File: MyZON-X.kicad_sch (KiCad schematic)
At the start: 29 parts, among them J1 Connector ZX81, J2 Audio, SW1 SW_DIP_x03, U1 AY-3-8910, U2.1 74HCT74, U3.1 74HCT08, U4.1 74HCT11, U5.1 74HCT02

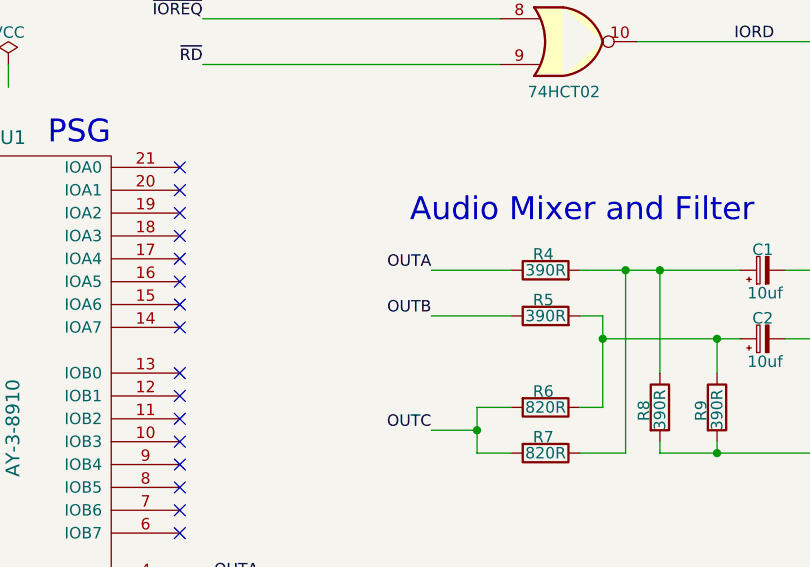
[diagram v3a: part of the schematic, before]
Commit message: Channged Channel A and B over on the audio mixer as they would have been the wrong way to what I intended.
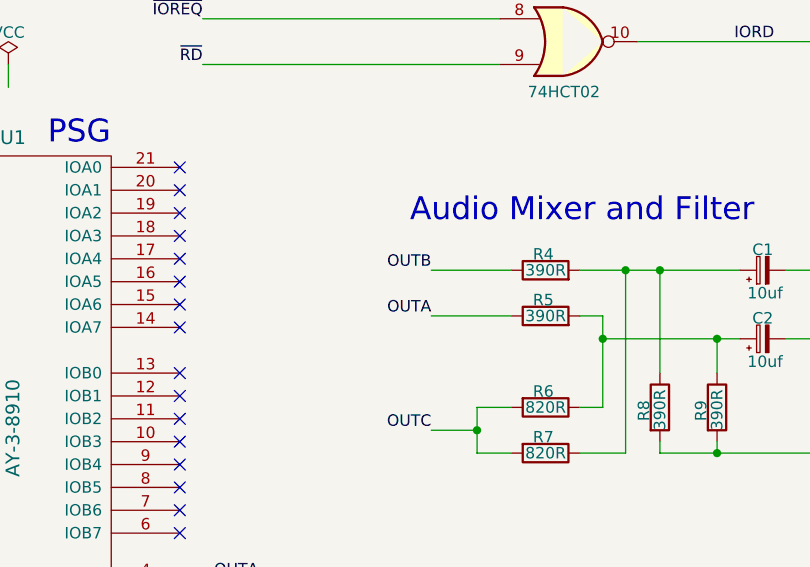
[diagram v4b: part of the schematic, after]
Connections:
- net OUTA: now also R5.1; no longer R4.1
- net OUTB: now also R4.1; no longer R5.1
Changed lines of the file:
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@@
 		)
 	)
-	(label "OUTB"
+	(label "OUTA"
 		(at 130.81 130.81 180)
 		(effects
@@
 		)
 	)
-	(label "OUTA"
+	(label "OUTB"
 		(at 130.81 125.73 180)
 		(effects

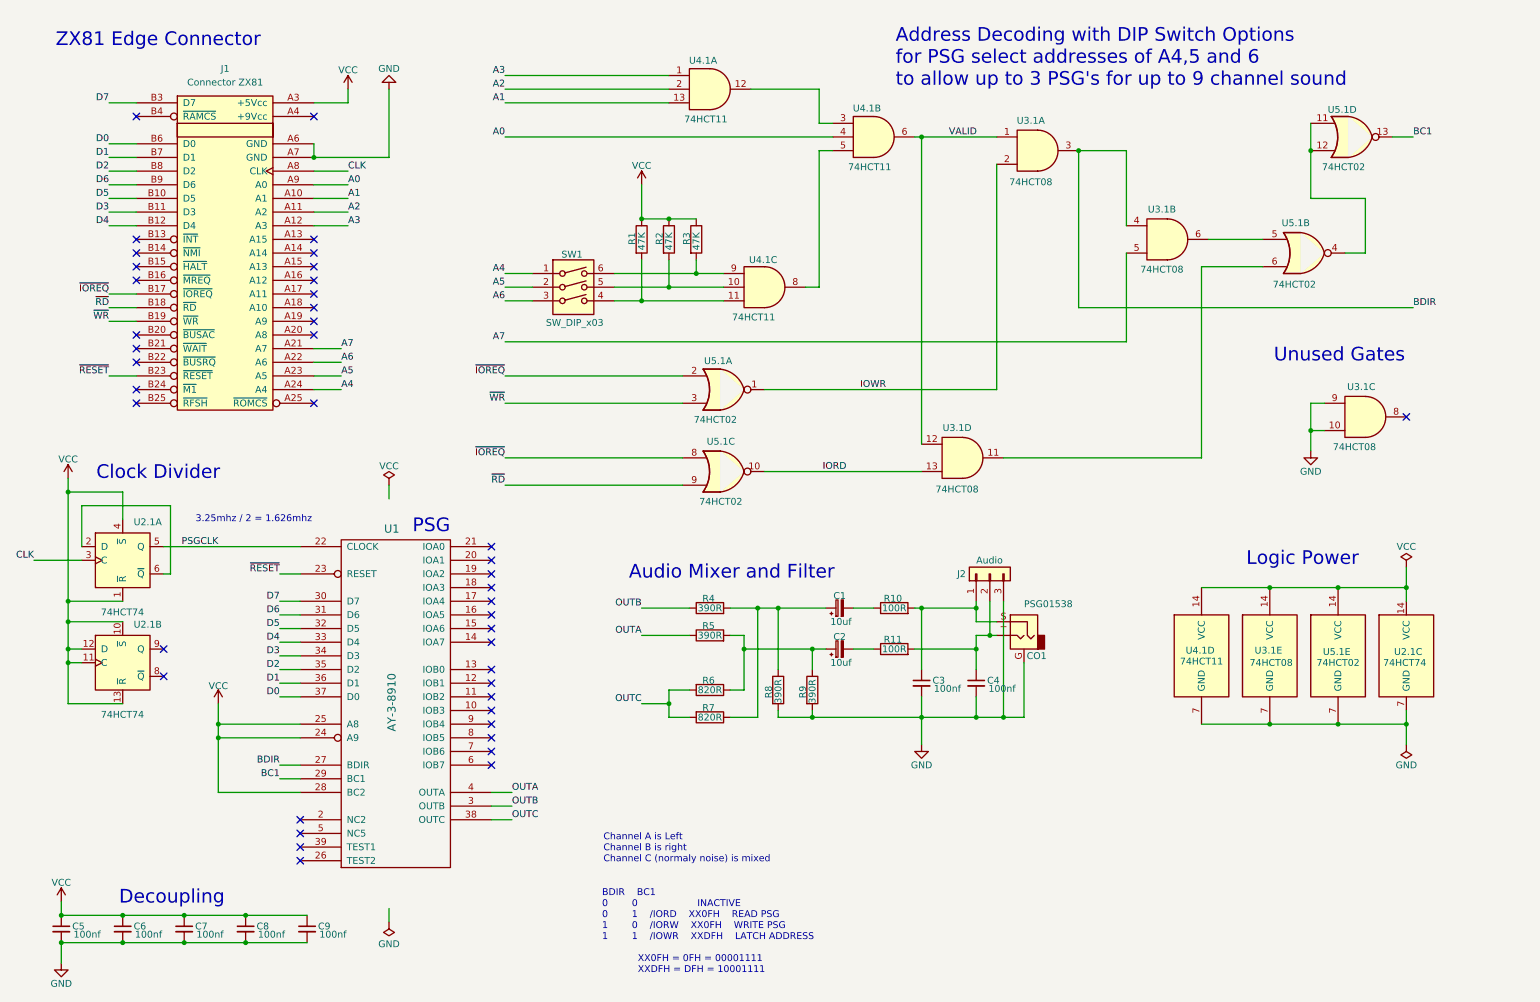
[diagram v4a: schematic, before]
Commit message: added just two power inputs for +5Vcc to VCC and GND to GND Created commented ERC warning as +5Vcc and GND are bidirectional  by design. Move a few of the text comments to make the schematic look neater Exported an updated PDF of the schematic
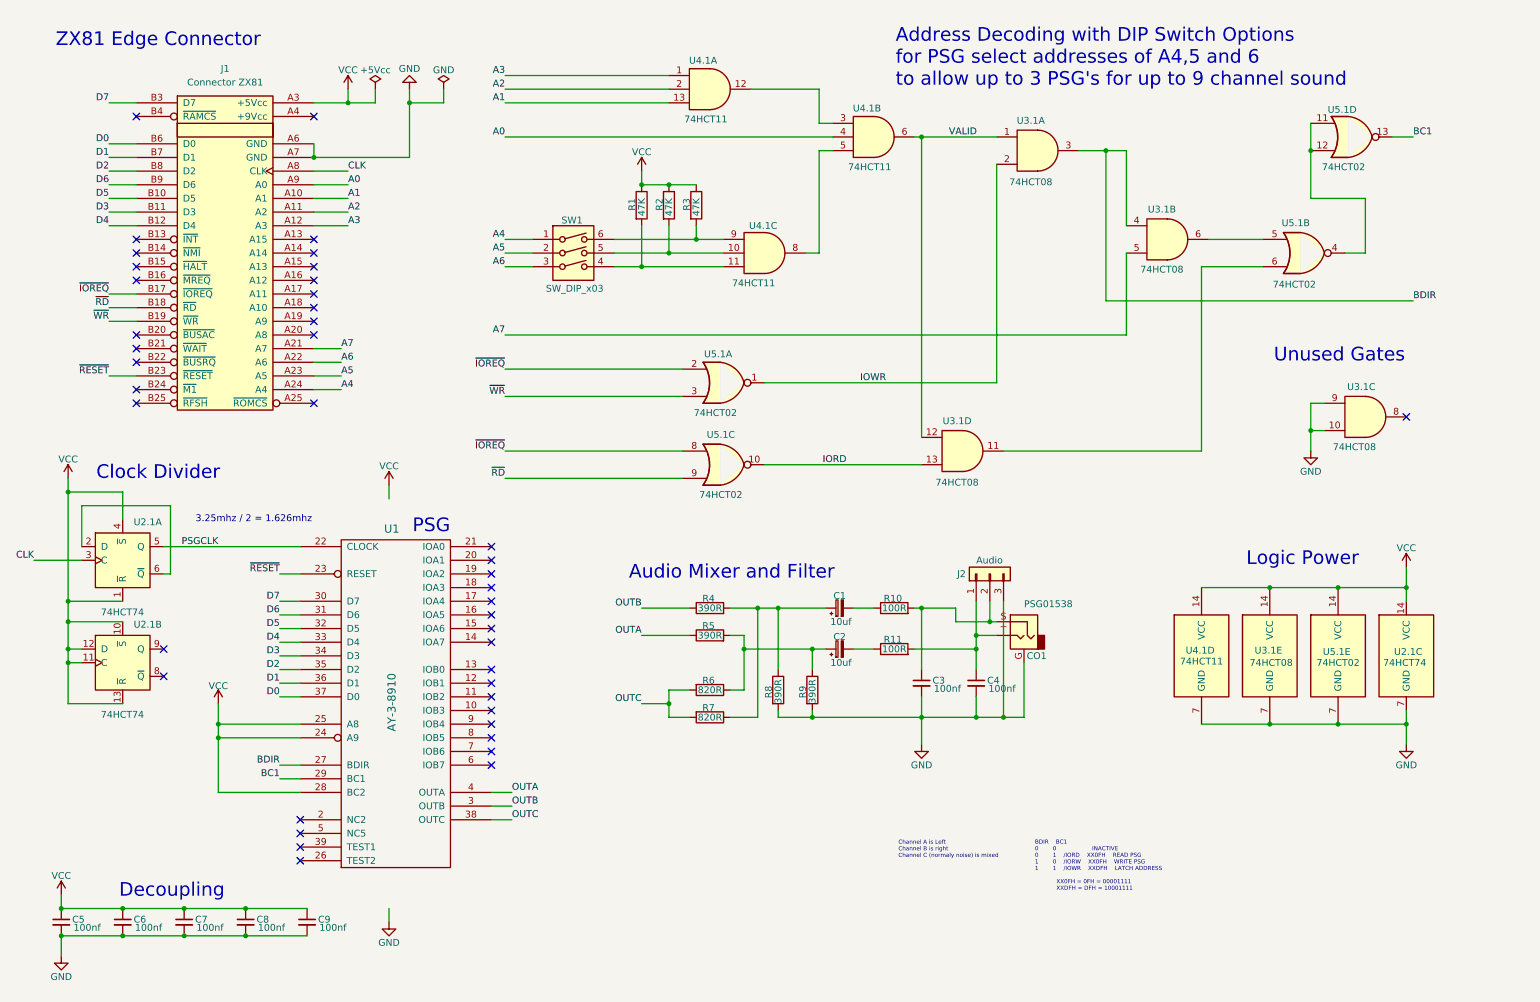
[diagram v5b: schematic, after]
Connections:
- net GND: now also U2.1.7 (GND), U3.1.7 (GND), U4.1.7 (GND), U5.1.7 (GND)
- net VCC: now also U2.1.14 (VCC), U3.1.14 (VCC), U4.1.14 (VCC), U5.1.14 (VCC)
- net at C4.1, CO1.T, R11.2: now also J2.1 (Pin_1); no longer J2.2 (Pin_2)
- net at C3.1, CO1.S, R10.2: now also J2.2 (Pin_2); no longer J2.1 (Pin_1)
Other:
- moved on the sheet: C5, C6, C7, C8, C9, R1, R2, R3, SW1, U3.1D, U4.1C, U5.1A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

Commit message: Started PCB
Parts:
- C1, C2: footprint (none) -> Capacitor_THT:CP_Radial_D5.0mm_P2.00mm
- C3, C4, C5, C6, C7, C8, C9: footprint (none) -> Capacitor_THT:C_Disc_D3.0mm_W1.6mm_P2.50mm
- CO1: footprint (none) -> Connector_Audio:Jack_3.5mm_CUI_SJ1-3533NG_Horizontal_CircularHoles
- J1: footprint (none) -> ZX81_FOOTPRINT:EDGE ZX81 TOP
- J2: footprint (none) -> Connector_PinHeader_2.54mm:PinHeader_1x03_P2.54mm_Vertical
- R1, R10, R11, R2, R3, R4, R5, R6, R7, R8, R9: footprint (none) -> Resistor_THT:R_Axial_DIN0207_L6.3mm_D2.5mm_P7.62mm_Horizontal
- SW1: footprint (none) -> Button_Switch_SMD:SW_DIP_SPSTx03_Slide_9.78x9.8mm_W8.61mm_P2.54mm
- U1: footprint (none) -> Package_DIP:DIP-40_W15.24mm_Socket
- U2.1, U3.1, U4.1, U5.1: footprint (none) -> Package_DIP:DIP-14_W7.62mm_Socket
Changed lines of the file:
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@@
 			)
 		)
-		(property "Footprint" ""
+		(property "Footprint" "Package_DIP:DIP-14_W7.62mm_Socket"
 			(at 34.29 135.89 0)
 			(effects
@@
 			)
 		)
-		(property "Footprint" ""
+		(property "Footprint" "Package_DIP:DIP-14_W7.62mm_Socket"
 			(at 265.43 90.17 0)
 			(effects
@@
 			)
 		)
-		(property "Footprint" ""
+		(property "Footprint" "Capacitor_THT:CP_Radial_D5.0mm_P2.00mm"
 			(at 167.64 133.35 0)
 			(effects
@@
 			)
 		)
-		(property "Footprint" ""
+		(property "Footprint" "Resistor_THT:R_Axial_DIN0207_L6.3mm_D2.5mm_P7.62mm_Horizontal"
 			(at 177.8 135.128 90)
 			(effects
@@
 			)
 		)
-		(property "Footprint" ""
+		(property "Footprint" "Package_DIP:DIP-14_W7.62mm_Socket"
 			(at 228.6 57.15 0)
 			(effects
@@
 			)
 		)
-		(property "Footprint" ""
+		(property "Footprint" "Package_DIP:DIP-14_W7.62mm_Socket"
 			(at 260.35 134.62 0)
 			(effects
@@
 			)
 		)
-		(property "Footprint" ""
+		(property "Footprint" "Package_DIP:DIP-40_W15.24mm_Socket"
 			(at 85.09 143.51 0)
 			(effects
@@
 					(size 1.524 1.524)
 				)
+				(hide yes)
 			)
 		)
@@
 			)
 		)
-		(property "Footprint" ""
+		(property "Footprint" "Resistor_THT:R_Axial_DIN0207_L6.3mm_D2.5mm_P7.62mm_Horizontal"
 			(at 143.51 132.588 90)
 			(effects
@@
 			)
 		)
-		(property "Footprint" ""
+		(property "Footprint" "Package_DIP:DIP-14_W7.62mm_Socket"
 			(at 153.67 59.69 0)
 			(effects
@@
 			)
 		)
-		(property "Footprint" ""
+		(property "Footprint" "Package_DIP:DIP-14_W7.62mm_Socket"
 			(at 190.5 96.52 0)
 			(effects
@@
 			)
 		)
-		(property "Footprint" ""
+		(property "Footprint" "Package_DIP:DIP-14_W7.62mm_Socket"
 			(at 34.29 116.84 0)
 			(effects
@@
 			)
 		)
-		(property "Footprint" ""
+		(property "Footprint" "Connector_Audio:Jack_3.5mm_CUI_SJ1-3533NG_Horizontal_CircularHoles"
 			(at 201.93 130.81 0)
 			(effects
@@
 			)
 		)
-		(property "Footprint" ""
+		(property "Footprint" "Resistor_THT:R_Axial_DIN0207_L6.3mm_D2.5mm_P7.62mm_Horizontal"
 			(at 154.432 140.97 90)
 			(effects
@@
 			)
 		)
-		(property "Footprint" ""
+		(property "Footprint" "Resistor_THT:R_Axial_DIN0207_L6.3mm_D2.5mm_P7.62mm_Horizontal"
 			(at 177.8 127.508 90)
 			(effects
@@
 			)
 		)
-		(property "Footprint" ""
+		(property "Footprint" "Package_DIP:DIP-14_W7.62mm_Socket"
 			(at 146.05 83.82 0)
 			(effects
@@
 			)
 		)
-		(property "Footprint" ""
+		(property "Footprint" "Resistor_THT:R_Axial_DIN0207_L6.3mm_D2.5mm_P7.62mm_Horizontal"
 			(at 129.032 50.8 90)
 			(effects
@@
 			)
 		)
-		(property "Footprint" ""
+		(property "Footprint" "Resistor_THT:R_Axial_DIN0207_L6.3mm_D2.5mm_P7.62mm_Horizontal"
 			(at 143.51 139.192 90)
 			(effects
@@
 			)
 		)
-		(property "Footprint" ""
+		(property "Footprint" "Resistor_THT:R_Axial_DIN0207_L6.3mm_D2.5mm_P7.62mm_Horizontal"
 			(at 160.782 140.97 90)
 			(effects
@@
 			)
 		)
-		(property "Footprint" ""
+		(property "Footprint" "Package_DIP:DIP-14_W7.62mm_Socket"
 			(at 247.65 134.62 0)
 			(effects
@@
 			)
 		)
-		(property "Footprint" ""
+		(property "Footprint" "Capacitor_THT:CP_Radial_D5.0mm_P2.00mm"
 			(at 167.64 125.73 0)
 			(effects
@@
 			)
 		)
-		(property "Footprint" ""
+		(property "Footprint" "Connector_PinHeader_2.54mm:PinHeader_1x03_P2.54mm_Vertical"
 			(at 195.58 119.38 0)
 			(effects
@@
 			)
 		)
-		(property "Footprint" ""
+		(property "Footprint" "Button_Switch_SMD:SW_DIP_SPSTx03_Slide_9.78x9.8mm_W8.61mm_P2.54mm"
 			(at 118.11 62.23 0)
 			(effects
@@
 			)
 		)
-		(property "Footprint" ""
+		(property "Footprint" "Package_DIP:DIP-14_W7.62mm_Socket"
 			(at 234.95 134.62 0)
 			(effects
@@
 			)
 		)
-		(property "Footprint" ""
+		(property "Footprint" "Package_DIP:DIP-14_W7.62mm_Socket"
 			(at 262.89 38.1 0)
 			(effects
@@
 			)
 		)
-		(property "Footprint" ""
+		(property "Footprint" "Capacitor_THT:C_Disc_D3.0mm_W1.6mm_P2.50mm"
 			(at 68.58 184.15 0)
 			(effects
@@
 			)
 		)
-		(property "Footprint" ""
+		(property "Footprint" "Package_DIP:DIP-14_W7.62mm_Socket"
 			(at 254 59.69 0)
 			(effects
@@
 			)
 		)
-		(property "Footprint" ""
+		(property "Footprint" "Resistor_THT:R_Axial_DIN0207_L6.3mm_D2.5mm_P7.62mm_Horizontal"
 			(at 143.51 127.508 90)
 			(effects
@@
 			)
 		)
-		(property "Footprint" ""
+		(property "Footprint" "Package_DIP:DIP-14_W7.62mm_Socket"
 			(at 204.47 40.64 0)
 			(effects
@@
 			)
 		)
-		(property "Footprint" ""
+		(property "Footprint" "Package_DIP:DIP-14_W7.62mm_Socket"
 			(at 273.05 134.62 0)
 			(effects
@@
 			)
 		)
-		(property "Footprint" ""
+		(property "Footprint" "Capacitor_THT:C_Disc_D3.0mm_W1.6mm_P2.50mm"
 			(at 182.88 139.7 0)
 			(effects
@@
 			)
 		)
-		(property "Footprint" ""
+		(property "Footprint" "Resistor_THT:R_Axial_DIN0207_L6.3mm_D2.5mm_P7.62mm_Horizontal"
 			(at 143.51 144.272 90)
 			(effects
@@
 			)
 		)
-		(property "Footprint" ""
+		(property "Footprint" "Capacitor_THT:C_Disc_D3.0mm_W1.6mm_P2.50mm"
 			(at 193.04 139.7 0)
 			(effects
@@
 			)
 		)
-		(property "Footprint" ""
+		(property "Footprint" "Resistor_THT:R_Axial_DIN0207_L6.3mm_D2.5mm_P7.62mm_Horizontal"
 			(at 134.112 50.8 90)
 			(effects
@@
 			)
 		)
-		(property "Footprint" ""
+		(property "Footprint" "Capacitor_THT:C_Disc_D3.0mm_W1.6mm_P2.50mm"
 			(at 22.86 184.15 0)
 			(effects
@@
 			)
 		)
-		(property "Footprint" ""
+		(property "Footprint" "ZX81_FOOTPRINT:EDGE ZX81 TOP"
 			(at 53.34 57.15 0)
 			(effects
@@
 			)
 		)
-		(property "Footprint" ""
+		(property "Footprint" "Capacitor_THT:C_Disc_D3.0mm_W1.6mm_P2.50mm"
 			(at 34.29 184.15 0)
 			(effects
@@
 			)
 		)
-		(property "Footprint" ""
+		(property "Footprint" "Resistor_THT:R_Axial_DIN0207_L6.3mm_D2.5mm_P7.62mm_Horizontal"
 			(at 139.192 50.8 90)
 			(effects
@@
 			)
 		)
-		(property "Footprint" ""
+		(property "Footprint" "Capacitor_THT:C_Disc_D3.0mm_W1.6mm_P2.50mm"
 			(at 45.72 184.15 0)
 			(effects
@@
 			)
 		)
-		(property "Footprint" ""
+		(property "Footprint" "Package_DIP:DIP-14_W7.62mm_Socket"
 			(at 143.51 29.21 0)
 			(effects
@@
 			)
 		)
-		(property "Footprint" ""
+		(property "Footprint" "Capacitor_THT:C_Disc_D3.0mm_W1.6mm_P2.50mm"
 			(at 57.15 184.15 0)
 			(effects
@@
 			)
 		)
-		(property "Footprint" ""
+		(property "Footprint" "Package_DIP:DIP-14_W7.62mm_Socket"
 			(at 173.99 38.1 0)
 			(effects
@@
 			)
 		)
-		(property "Footprint" ""
+		(property "Footprint" "Package_DIP:DIP-14_W7.62mm_Socket"
 			(at 146.05 99.06 0)
 			(effects

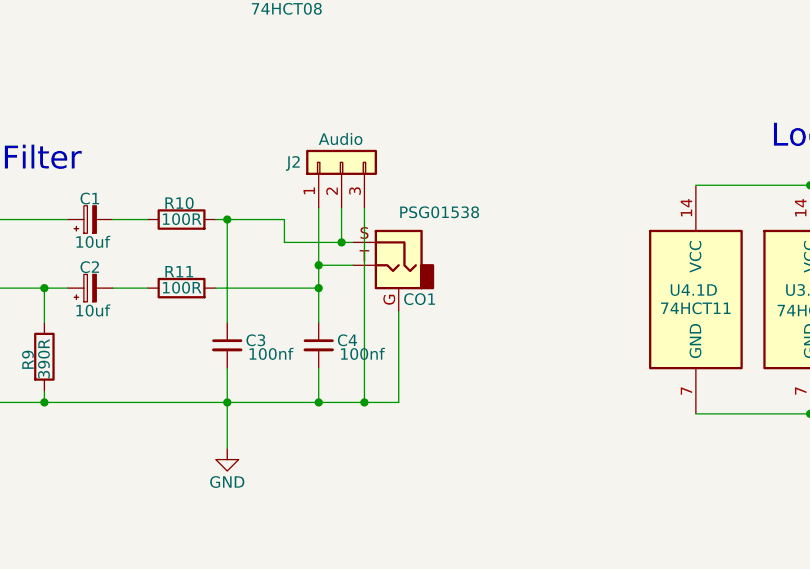
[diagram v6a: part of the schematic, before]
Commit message: Added Auto Jack Added Board outline Layed out some components in Board outline
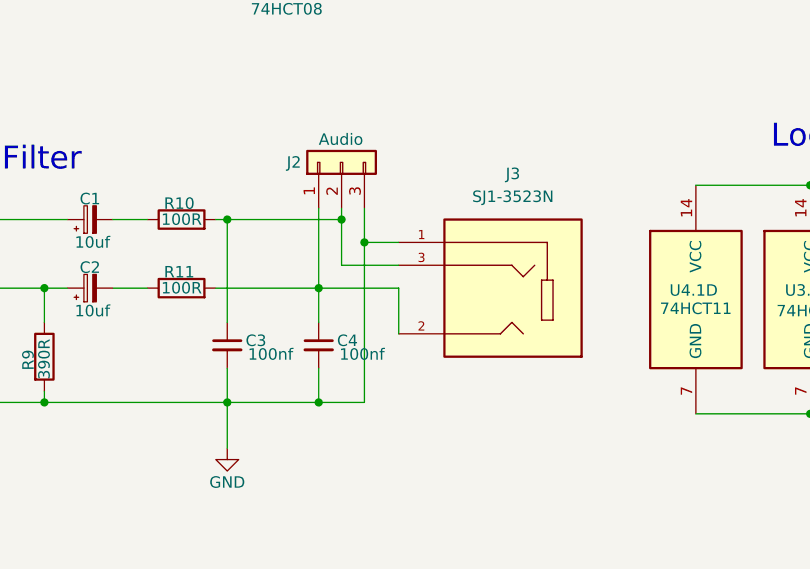
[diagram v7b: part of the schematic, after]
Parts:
- removed CO1: PSG01538, Connector_Audio:Jack_3.5mm_CUI_SJ1-3533NG_Horizontal_CircularHoles, symbol Connector_Audio:AudioJack2_Ground
- added J3: SJ1-3523N, AudioJack:CUI_SJ1-3523N, symbol AudioJack:SJ1-3523N
- SW1: footprint Button_Switch_SMD:SW_DIP_SPSTx03_Slide_9.78x9.8mm_W8.61mm_P2.54mm -> Button_Switch_THT:SW_DIP_SPSTx03_Slide_9.78x9.8mm_W7.62mm_P2.54mm
- U1: footprint Package_DIP:DIP-40_W15.24mm_Socket -> Package_DIP:DIP-40_W15.24mm_LongPads
- U2.1, U3.1, U4.1, U5.1: footprint Package_DIP:DIP-14_W7.62mm_Socket -> Package_DIP:DIP-14_W10.16mm_LongPads
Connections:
- net GND: now also J3.1
- net at C4.1, J2.1 (Pin_1), R11.2: now also J3.2
- net at C3.1, J2.2 (Pin_2), R10.2: now also J3.3
